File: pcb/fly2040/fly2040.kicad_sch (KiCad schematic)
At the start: 48 parts, among them J1 Conn_01x02, J10 Conn_01x02, J2 Conn_01x02, J3 Conn_01x02, J4 Conn_01x02, J5 Conn_01x02, J6 Conn_01x02, J7 Conn_01x02, J8 Conn_01x06, J9 Conn_01x02, SW1 EVPAWED40, U1 RP2040, U2 W25Q16JVUXIQ, U3 RS0102YH8, U4 TPS613222ADBVR, X1 SMD-3225_4P_12.000MHZ_9PF

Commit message: Added more outputs. Improved board layout for panel. Added panel files
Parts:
- added J11: Conn_01x02, kicad_lceda:TH_Pads_1x02_P1.50mml, symbol Connector_Generic:Conn_01x02
- added J12: Conn_01x06, kicad_lceda:Pad_6Pin, symbol Connector_Generic:Conn_01x06
- added R12: 10k, R_0402_1005Metric, symbol jlcpcb-basic-resistor-0402:10k
- J1, J10, J2, J3, J4, J5, J6, J7, J9: now left out of the parts list
- L1: LCSC (none) -> C359305
- LED1: LCSC (none) -> C2909059
- R7: LCSC (none) -> C25744
- SW1: LCSC (none) -> C2858607
- U1: LCSC (none) -> C2040
- U2: LCSC (none) -> C2843335
- U3: LCSC (none) -> C783414
- U4: LCSC (none) -> C2071163
- X1: LCSC (none) -> C362368
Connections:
- net +3V3: now also J12.2 (Pin_2)
- net GND: now also R12.2
- net NS_19: now reaches U1.30 (GPIO19)
- net NS_19: now also J11.1 (Pin_1)
- net NS_20: now reaches U1.31 (GPIO20)
- net NS_20: now also J11.2 (Pin_2)
- net PAD_21: now reaches U1.32 (GPIO21)
- net PAD_21: now also J12.1 (Pin_1)
- net PAD_22: now reaches U1.34 (GPIO22)
- net PAD_22: now also J12.3 (Pin_3)
- net PAD_23: now reaches U1.35 (GPIO23)
- net PAD_23: now also J12.4 (Pin_4)
- net PAD_24: now reaches U1.36 (GPIO24)
- net PAD_24: now also J12.5 (Pin_5)
- net PAD_25: now reaches U1.37 (GPIO25)
- net PAD_25: now also J12.6 (Pin_6)
- net NS_14 renamed NS_CPU_PD
- net NS_CPU_PD: now also R12.1

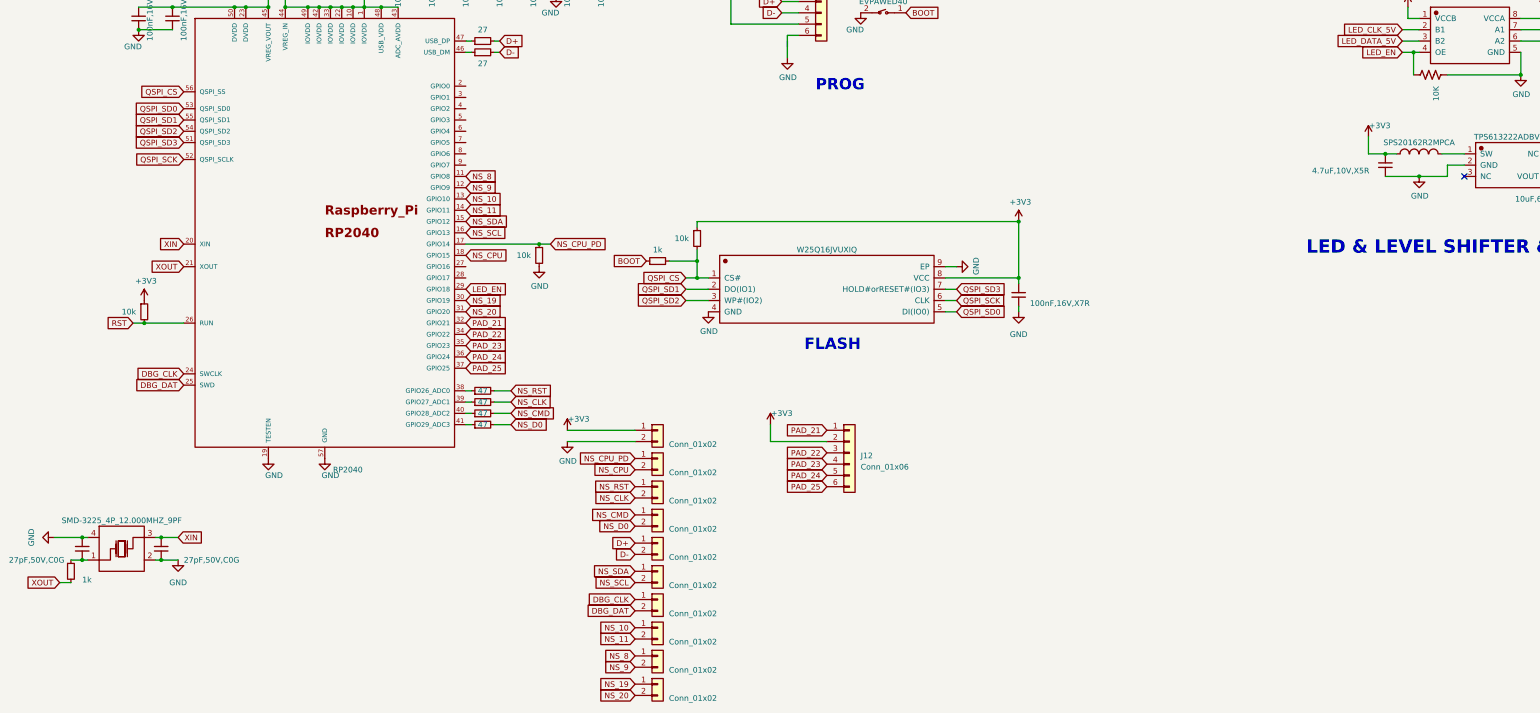
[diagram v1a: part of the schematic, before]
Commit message: Added tiny double sided (ds) board.
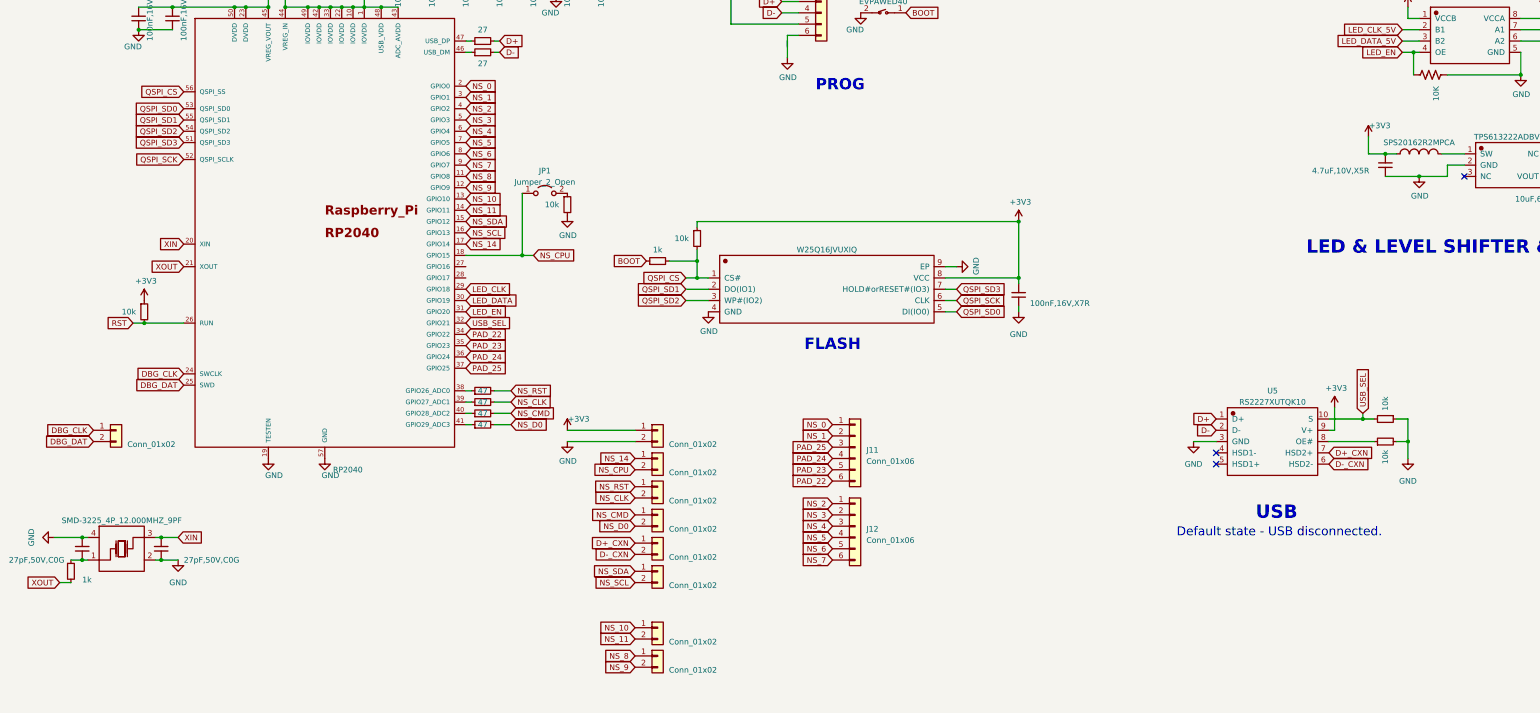
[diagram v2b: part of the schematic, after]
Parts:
- removed J11: Conn_01x02, kicad_lceda:TH_Pads_1x02_P1.50mml, symbol Connector_Generic:Conn_01x02
- added J11: Conn_01x06, kicad_lceda:Pad_6Pin, symbol Connector_Generic:Conn_01x06
- added JP1: Jumper_2_Open, kicad_lceda:SolderJumper-2_P1.3mm_Open_TrianglePad1.0x1.5mm_Sm, symbol Jumper:Jumper_2_Open
- added R13, R14: 10k, R_0402_1005Metric, symbol jlcpcb-basic-resistor-0402:10k
- added U5: RS2227XUTQK10, kicad_lceda:WQFN-10_L1.8-W1.4-P0.40-BL, symbol kicad_lceda:RS2227XUTQK10
- J7: footprint kicad_lceda:TH_Pads_1x02_P1.50mml -> kicad_lceda:PinHeader_Sm_1x02_P1.27mm_Vertical
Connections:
- net NS_19 is gone; now on net LED_DATA: U1.30 (GPIO19)
- net NS_20 is gone; now on net LED_EN: U1.31 (GPIO20)
- net +3V3: now also U5.9 (V+); no longer J12.2 (Pin_2)
- net D+: now also U5.1 (D+); no longer J5.1 (Pin_1)
- net D-: now also U5.2 (D-); no longer J5.2 (Pin_2)
- net GND: now also R13.1, R14.2, U5.3 (GND)
- net LED_CLK: now also U1.29 (GPIO18)
- net LED_EN: no longer U1.29 (GPIO18)
- net NS_CPU: now also JP1.1 (A)
- net PAD_22: now also J11.6 (Pin_6); no longer J12.3 (Pin_3)
- net PAD_23: now also J11.5 (Pin_5); no longer J12.4 (Pin_4)
- net PAD_24: now also J11.4 (Pin_4); no longer J12.5 (Pin_5)
- net PAD_25: now also J11.3 (Pin_3); no longer J12.6 (Pin_6)
- net NS_0: now reaches U1.2 (GPIO0)
- net NS_0: now also J11.1 (Pin_1)
- net NS_1: now reaches U1.3 (GPIO1)
- net NS_1: now also J11.2 (Pin_2)
- net NS_2: now reaches U1.4 (GPIO2)
- net NS_2: now also J12.1 (Pin_1)
- net NS_3: now reaches U1.5 (GPIO3)
- net NS_3: now also J12.2 (Pin_2)
- net NS_4: now reaches U1.6 (GPIO4)
- net NS_4: now also J12.3 (Pin_3)
- net NS_5: now reaches U1.7 (GPIO5)
- net NS_5: now also J12.4 (Pin_4)
- net NS_6: now reaches U1.8 (GPIO6)
- net NS_6: now also J12.5 (Pin_5)
- net NS_7: now reaches U1.9 (GPIO7)
- net NS_7: now also J12.6 (Pin_6)
- net NS_CPU_PD renamed NS_14
- net NS_14: no longer R12.1
- net PAD_21 renamed USB_SEL
- net USB_SEL: now also R13.2, U5.10 (S); no longer J12.1 (Pin_1)
- new net: JP1.2 (B), R12.1
- new net: R14.1, U5.8 (OE#)
- new net D+_CXN: J5.1 (Pin_1), U5.7 (HSD2+)
- new net D-_CXN: J5.2 (Pin_2), U5.6 (HSD2-)
- no-connect marks 4 -> 6
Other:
- note added: "Default state - USB disconnected."
- note added: "USB"

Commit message: Updated main board with bus isolation ICs
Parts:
- removed #C16: 22uF,25V,X5R, C_0805_2012Metric, symbol jlcpcb-basic-capacitor-0805:22uF,25V,X5R
- removed C15: 4.7uF,10V,X5R, C_0402_1005Metric, symbol jlcpcb-basic-capacitor-0402:4.7uF,10V,X5R
- removed C16, C17: 10uF,6.3V,X5R, C_0402_1005Metric, symbol jlcpcb-basic-capacitor-0402:10uF,6.3V,X5R
- removed C18: 2.2uF,6.3V,X5R, C_0402_1005Metric, symbol jlcpcb-basic-capacitor-0402:2.2uF,6.3V,X5R
- removed J7: Conn_01x02, kicad_lceda:PinHeader_Sm_1x02_P1.27mm_Vertical, symbol Connector_Generic:Conn_01x02
- removed L1: SPS20162R2MPCA, kicad_lceda:IND-SMD_L2.0-W1.6, symbol kicad_lceda:SPS20162R2MPCA
- removed LED1: SK9822-EC20, kicad_lceda:LED-SMD_6P-L2.0-W2.0-P0.80-TL, symbol kicad_lceda:SK9822-EC20
- removed R10, R11, R8, R9: 47, R_0402_1005Metric, symbol jlcpcb-basic-resistor-0402:47
- removed R7: 10K, Resistor_SMD:R_0402_1005Metric, symbol ESP32+TFT-rescue:R_US-M9J_RLC-ESP32+TFT-rescue-ESP32+TFT-rescue
- removed U3: RS0102YH8, kicad_lceda:SOT-23-8_L3.0-W1.7-P0.65-LS2.8-BL, symbol kicad_lceda:RS0102YH8
- removed U4: TPS613222ADBVR, kicad_lceda:TSOT-23-5_L2.9-W1.6-P0.95-LS2.8-BR, symbol kicad_lceda:TPS613222ADBVR
- added JP2: Jumper_2_Open, kicad_lceda:SolderJumper-2_P1.3mm_Open_TrianglePad1.0x1.5mm_Sm, symbol Jumper:Jumper_2_Open
- added R15, R16, R7, R8, R9: 10k, R_0402_1005Metric, symbol jlcpcb-basic-resistor-0402:10k
- added U3: RT9078-25GJ5, kicad_lceda:TSOT-23-5_L2.9-W1.6-P0.95-LS2.8-BL, symbol kicad_lceda:RT9078-25GJ5
- added U4: RT9080-33GJ5, kicad_lceda:TSOT-23-5_L2.9-W1.6-P0.95-LS2.8-BL, symbol kicad_lceda:RT9080-33GJ5
- added U6: SN74CBTLV3125RGYR, kicad_lceda:VQFN-14_L3.5-W3.5-P0.50-BL-EP, symbol kicad_lceda:SN74CBTLV3125RGYR
- added U7: XL-1010RGBC-WS2812B, kicad_lceda:LED-SMD_4P-L1.0-W1.0-TL_XL-1010RGBC-WS2812B, symbol kicad_lceda:XL-1010RGBC-WS2812B
- added U8: 74LVC1GU04GV,125, kicad_lceda:SC-74A-5_L2.9-W1.6-P0.95-LS2.8-BL, symbol kicad_lceda:74LVC1GU04GV,125
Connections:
- net LED_CLK is gone; now on net USB_SEL: U1.29 (GPIO18)
- net +3V3: now also U3.1 (VIN), U4.5 (VOUT), U7.2 (VDD), U8.5 (VCC); no longer J8.5 (Pin_5)
- net +5V: now also J8.5 (Pin_5), R8.1, U4.1 (VIN)
- net GND: now also J11.3 (Pin_3), R15.1, R7.2, R9.2, U3.2 (GND), U4.2 (GND), U6.15 (PAD), U6.7 (GND), U7.3 (GND), U8.3 (GND)
- net LED_DATA: now also U1.27 (GPIO16), U7.4 (DIN); no longer U1.30 (GPIO19)
- net NS_CLK: now also U1.39 (GPIO27_ADC1), U6.5 (2A); no longer J3.2 (Pin_2)
- net NS_CMD: now also U1.40 (GPIO28_ADC2), U6.9 (3A); no longer J4.1 (Pin_1)
- net NS_D0: now also U1.41 (GPIO29_ADC3), U6.12 (4A); no longer J4.2 (Pin_2)
- net NS_RST: now also U1.38 (GPIO26_ADC0), U6.2 (1A); no longer J3.1 (Pin_1)
- net USB_SEL: no longer U1.32 (GPIO21)
- net PAD_17: now reaches U1.28 (GPIO17)
- net LED_EN renamed PAD_20
- net PAD_25 renamed BOARD_DET
- net BOARD_DET: now also R7.1; no longer J11.3 (Pin_3)
- new net: R8.2, U4.3 (EN)
- new net: JP2.2 (B), R9.1
- new net: R16.1, U8.4 (Y)
- new net +2V5: U3.5 (VOUT), U6.14 (VCC)
- new net MMC_SEL: R15.2, U1.30 (GPIO19), U3.3 (EN), U8.2 (A)
- new net MMC_SEL_INV: R16.2, U6.1 (1OE#), U6.10 (3OE#), U6.13 (4OE#), U6.4 (2OE#)
- new net NS_CLK_OUT: J3.2 (Pin_2), U6.6 (2B)
- new net NS_CMD_OUT: J4.1 (Pin_1), U6.8 (3B)
- new net NS_D0_OUT: J4.2 (Pin_2), U6.11 (4B)
- new net NS_RST_OUT: J3.1 (Pin_1), JP2.1 (A), U6.3 (1B)
- new net PAD_21: U1.32 (GPIO21)
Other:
- note removed: "LED & LEVEL SHIFTER & 5V BOOST"
- moved on the sheet: J11, J12
